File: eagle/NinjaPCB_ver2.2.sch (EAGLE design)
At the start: 60 parts, among them IC3 ANALOGSW_AD_SOT23-6, IC6 NAU7802, J2 ATX24, J3 HEATER, J4 HEATER_TEMP, Q1 S8550, Q2 IRF520NPBF, Q3 IRF520NPBF, Q4 S8550, Q5 IRF520NPBF, Q6 S8550, Q7 S8550, Q8 S8550, U1 CJT1117-3.3-SOT223

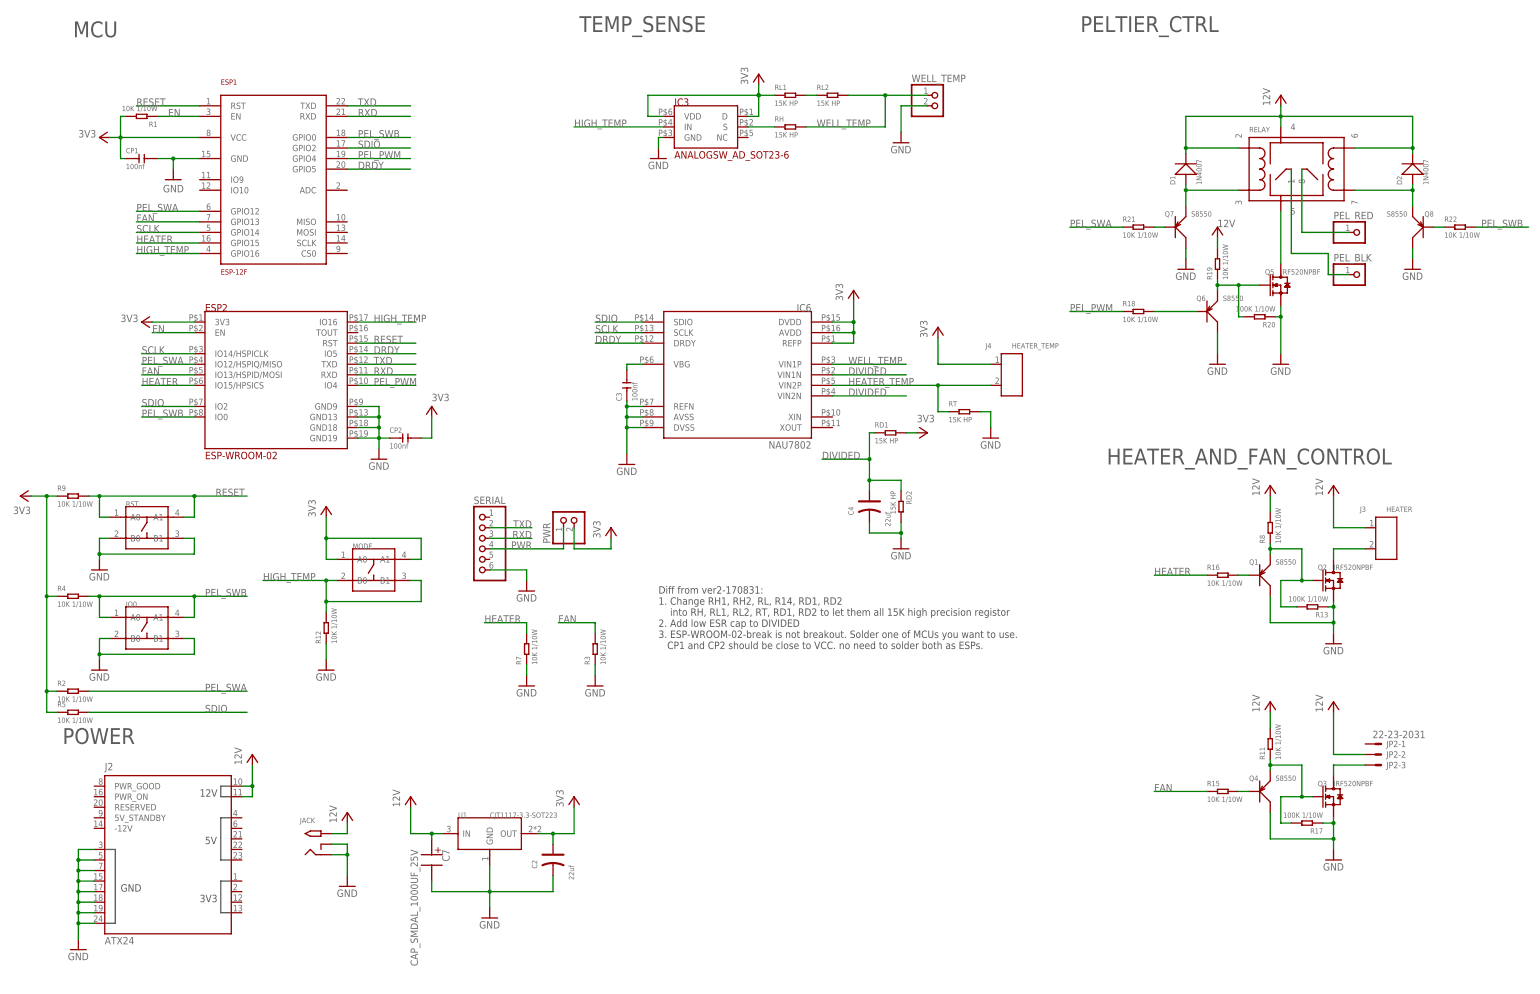
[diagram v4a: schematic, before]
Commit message: replace 2d data to ver2 dxf
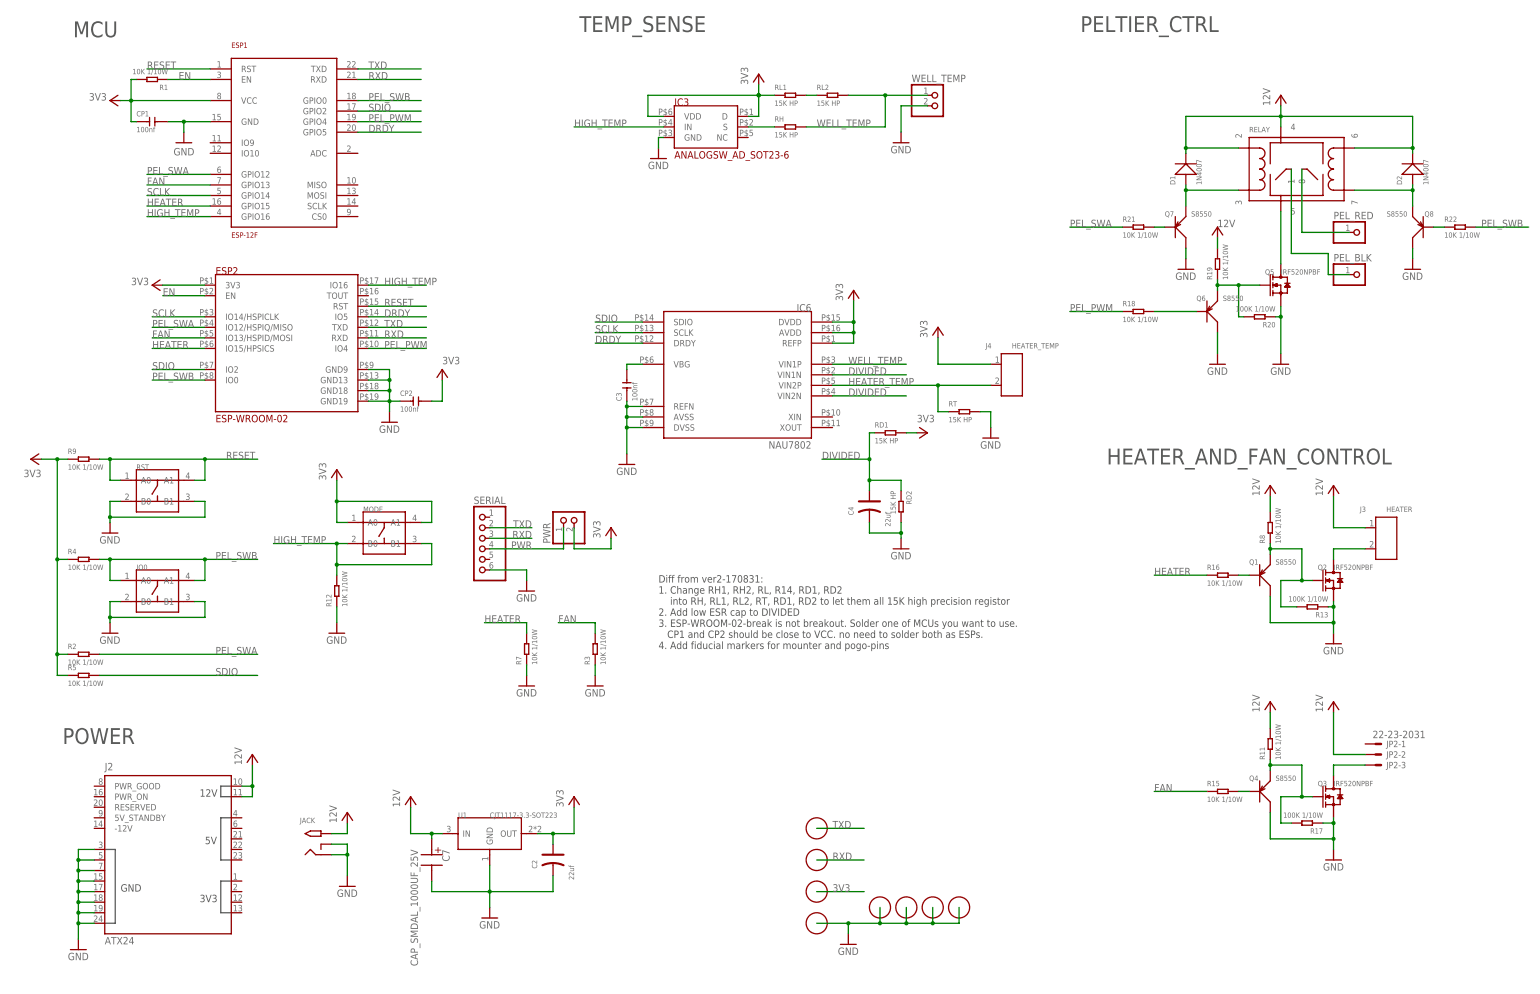
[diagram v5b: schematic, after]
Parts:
- added U$1, U$2, U$3, U$4, U$5, U$6, U$7, U$8: FIDUCIAL, adafruit:FIDUCIAL
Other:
- note added: "Diff from ver2-170831: 1. Change RH1, RH2, RL, R14, RD1, RD2 into RH, RL1, RL2, RT, RD1, RD2 to let them all 15K high precision registor 2. Add low ESR cap to DIVIDED 3. ESP-WROOM-02-break is not breakout. Solder one of MCUs you want to use. CP1 and CP2 should be close to VCC. no need to solder both as ESPs. 4. Add fiducial markers for mounter and pogo-pins"
- note removed: "Diff from ver2-170831: 1. Change RH1, RH2, RL, R14, RD1, RD2 into RH, RL1, RL2, RT, RD1, RD2 to let them all 15K high precision registor 2. Add low ESR cap to DIVIDED 3. ESP-WROOM-02-break is not breakout. Solder one of MCUs you want to use. CP1 and CP2 should be close to VCC. no need to solder both as ESPs."
- moved on the sheet: CP1, CP2, ESP1, ESP2, IO0, MODE, R1, R12, R2, R4, R5, R9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

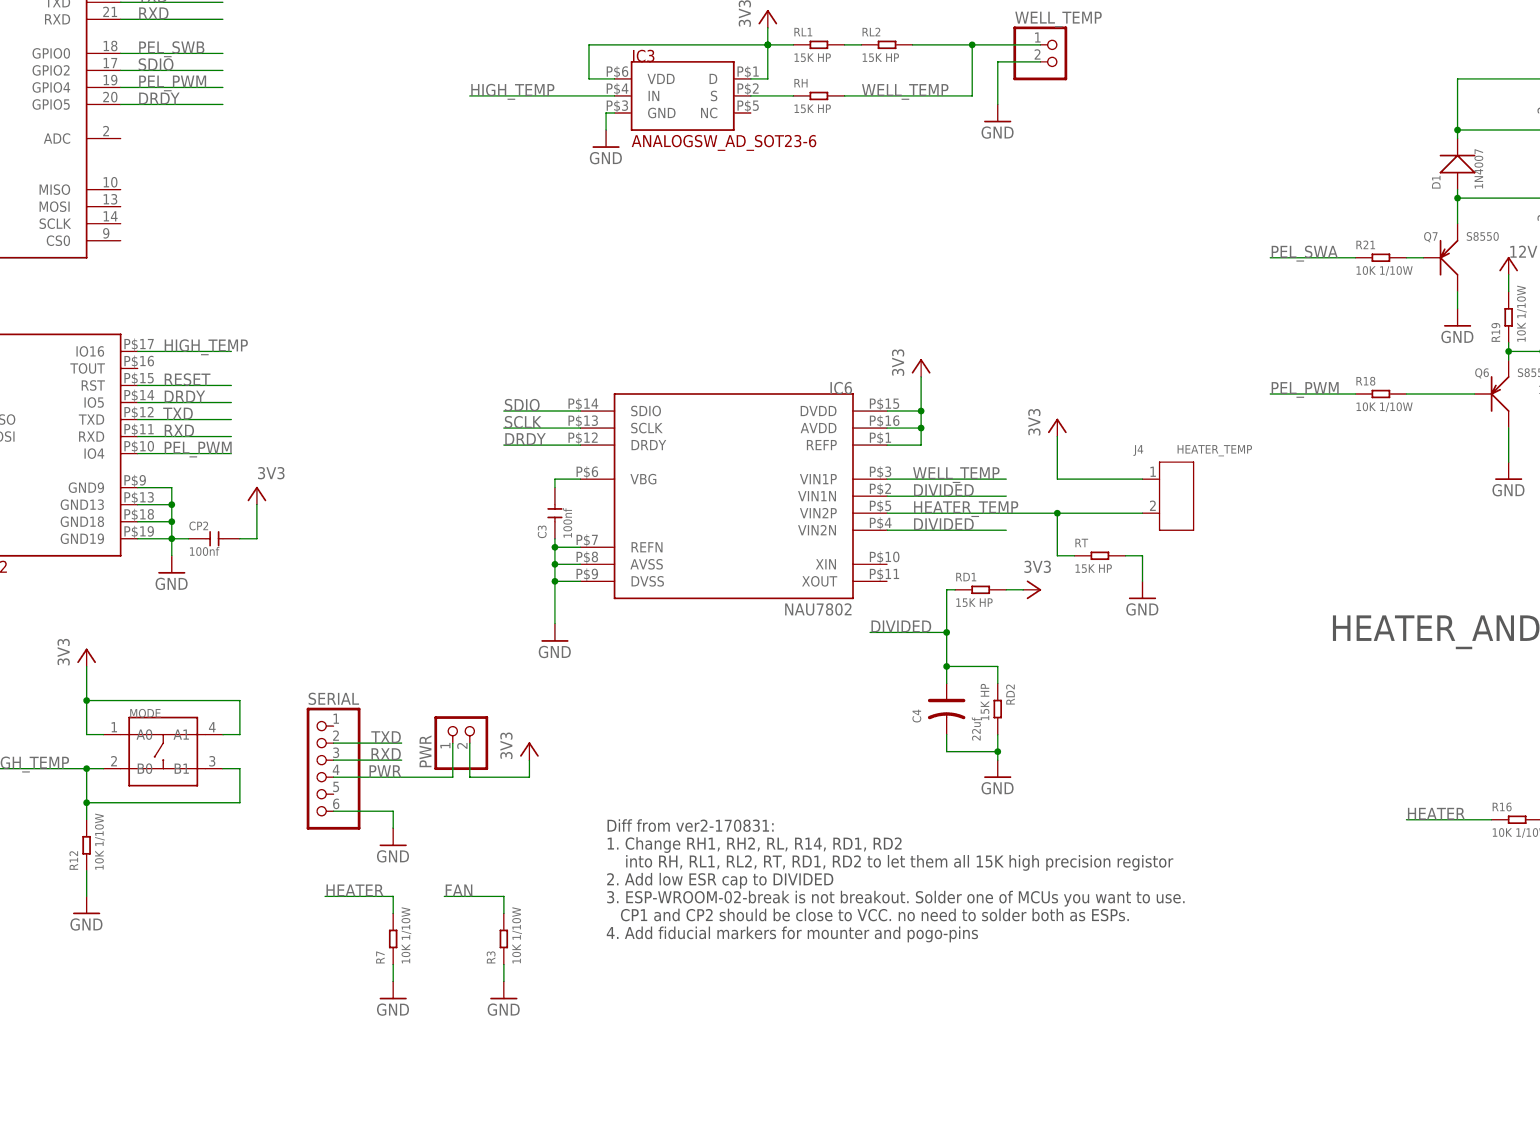
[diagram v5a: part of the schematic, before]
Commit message: add MODE jumper to use same source for 4x4 and 2x2
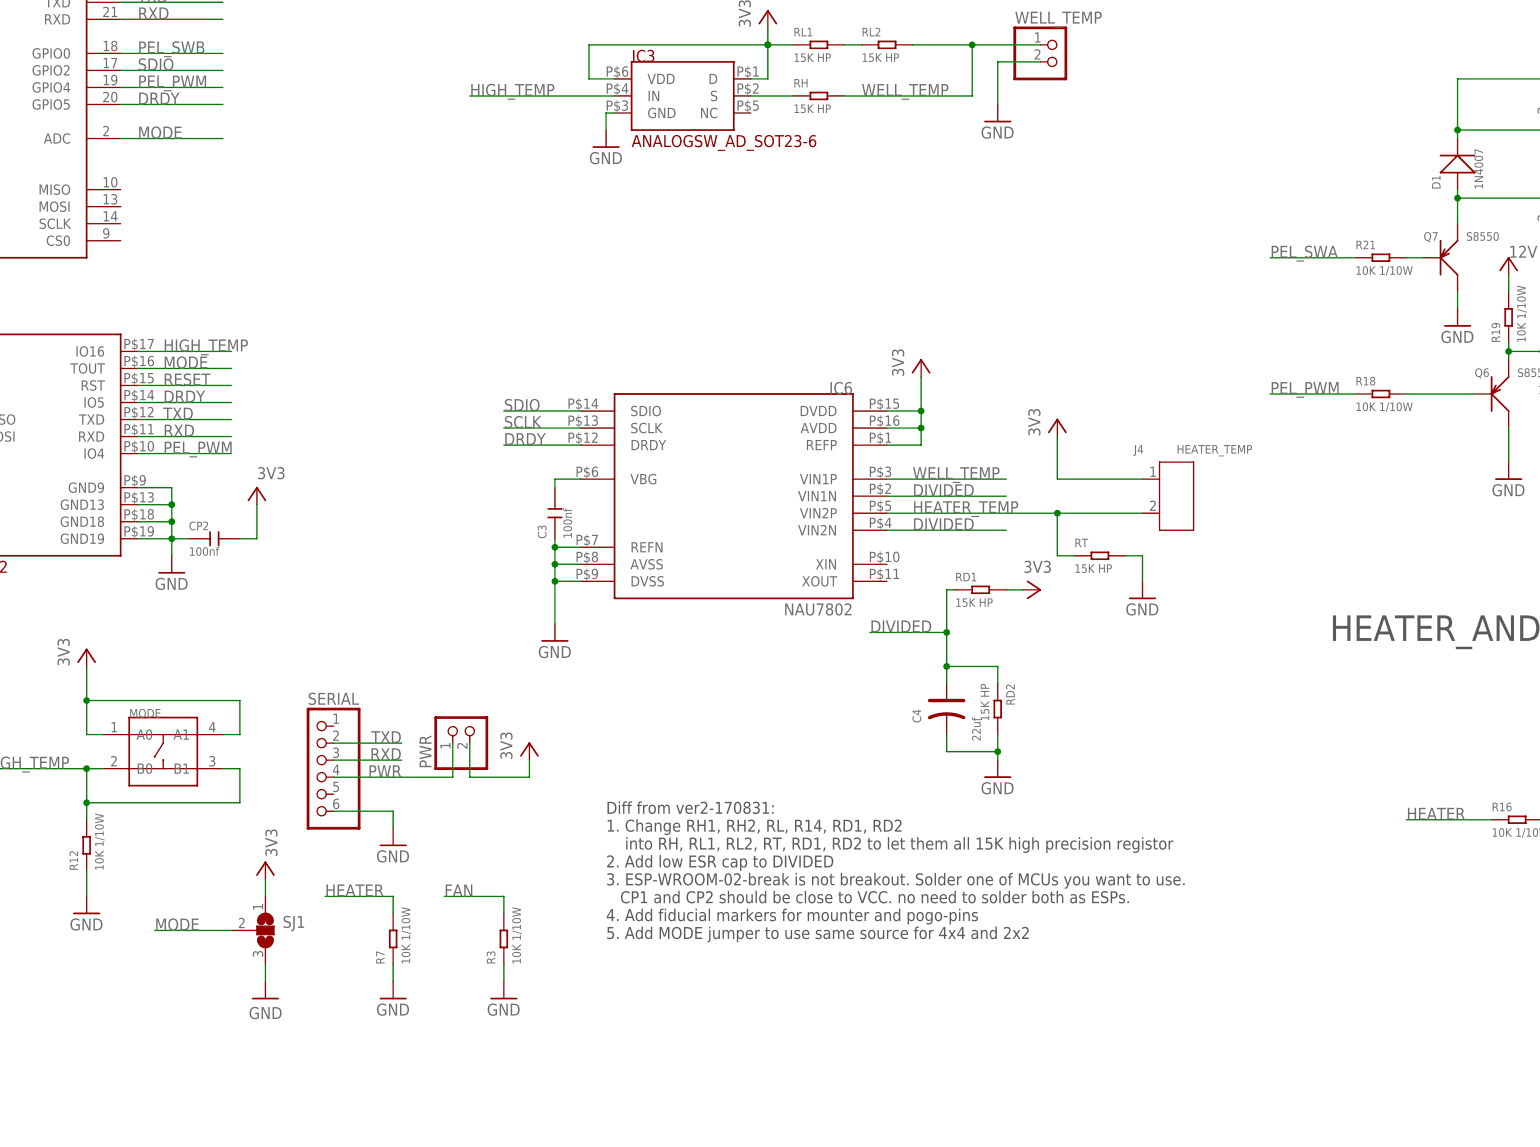
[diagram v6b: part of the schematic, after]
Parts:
- added SJ1: (no value), jumper:SJ2W
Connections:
- new net MODE: ESP1.ADC, ESP2.TOUT, SJ1.2
- net 3V3: now also SJ1.1
- net GND: now also SJ1.3
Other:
- note added: "Diff from ver2-170831: 1. Change RH1, RH2, RL, R14, RD1, RD2 into RH, RL1, RL2, RT, RD1, RD2 to let them all 15K high precision registor 2. Add low ESR cap to DIVIDED 3. ESP-WROOM-02-break is not breakout. Solder one of MCUs you want to use. CP1 and CP2 should be close to VCC. no need to solder both as ESPs. 4. Add fiducial markers for mounter and pogo-pins 5. Add MODE jumper to use same source f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"
- note removed: "Diff from ver2-170831: 1. Change RH1, RH2, RL, R14, RD1, RD2 into RH, RL1, RL2, RT, RD1, RD2 to let them all 15K high precision registor 2. Add low ESR cap to DIVIDED 3. ESP-WROOM-02-break is not breakout. Solder one of MCUs you want to use. CP1 and CP2 should be close to VCC. no need to solder both as ESPs. 4. Add fiducial markers for mounter and pogo-pins"

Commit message: add MooMoo ones
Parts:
- added R10, R14: 10K 1/10W, Seeed-Resistor:SMD-RES-10K-5%-1/10W(0603)
- added R6: 100K 1/10W, Seeed-Resistor:SMD-RES-100K-5%-1/10W(0603)
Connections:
- new net N$8: R10.1, R6.2, SJ1.1
- new net N$9: R14.2, SJ1.3
- net 3V3: now also R10.2; no longer SJ1.1
- net GND: now also R14.1, R6.1; no longer SJ1.3
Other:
- moved on the sheet: SJ1
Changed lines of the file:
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@@
 <part name="GND24" library="supply1" deviceset="GND" device=""/>
 <part name="SJ1" library="jumper" deviceset="SJ2W" device=""/>
+<part name="R6" library="Seeed-Resistor" deviceset="SMD-RES-100K-5%-1/10W(0603)" device="" value="100K 1/10W"/>
+<part name="R10" library="Seeed-Resistor" deviceset="SMD-RES-10K-5%-1/10W(0603)" device="" value="10K 1/10W"/>
+<part name="R14" library="Seeed-Resistor" deviceset="SMD-RES-10K-5%-1/10W(0603)" device="" value="10K 1/10W"/>
 </parts>
 <sheets>
@@
 <instance part="U$8" gate="G$1" x="205.74" y="48.26"/>
 <instance part="GND16" gate="1" x="213.36" y="20.32"/>
-<instance part="3V9" gate="VCC" x="116.84" y="102.87" smashed="yes">
-<attribute name="VALUE" x="116.84" y="107.95" size="1.778" layer="96" rot="R270"/>
+<instance part="3V9" gate="VCC" x="118.11" y="102.87" smashed="yes">
+<attribute name="VALUE" x="118.11" y="107.95" size="1.778" layer="96" rot="R270"/>
 </instance>
-<instance part="GND24" gate="1" x="116.84" y="82.55" smashed="yes">
-<attribute name="VALUE" x="119.38" y="81.28" size="1.778" layer="96" rot="R180"/>
+<instance part="GND24" gate="1" x="110.49" y="59.69" smashed="yes">
+<attribute name="VALUE" x="113.03" y="58.42" size="1.778" layer="96" rot="R180"/>
 </instance>
-<instance part="SJ1" gate="G$1" x="116.84" y="92.71"/>
+<instance part="SJ1" gate="G$1" x="110.49" y="78.74"/>
+<instance part="R6" gate="G$1" x="118.11" y="78.74" rot="R90"/>
+<instance part="R10" gate="G$1" x="118.11" y="93.98" rot="R90"/>
+<instance part="R14" gate="G$1" x="110.49" y="68.58" rot="R90"/>
 </instances>
 <busses>
@@
 </segment>
 <segment>
-<pinref part="SJ1" gate="G$1" pin="3"/>
 <pinref part="GND24" gate="1" pin="GND"/>
-<wire x1="116.84" y1="87.63" x2="116.84" y2="85.09" width="0.1524" layer="91"/>
+<pinref part="R6" gate="G$1" pin="1"/>
+<wire x1="110.49" y1="63.5" x2="110.49" y2="62.23" width="0.1524" layer="91"/>
+<wire x1="118.11" y1="74.93" x2="118.11" y2="63.5" width="0.1524" layer="91"/>
+<wire x1="118.11" y1="63.5" x2="110.49" y2="63.5" width="0.1524" layer="91"/>
+<pinref part="R14" gate="G$1" pin="1"/>
+<wire x1="110.49" y1="64.77" x2="110.49" y2="63.5" width="0.1524" layer="91"/>
+<junction x="110.49" y="63.5"/>
 </segment>
 </net>
@@
 </segment>
 <segment>
+<pinref part="R10" gate="G$1" pin="2"/>
 <pinref part="3V9" gate="VCC" pin="VCC"/>
-<pinref part="SJ1" gate="G$1" pin="1"/>
-<wire x1="116.84" y1="100.33" x2="116.84" y2="97.79" width="0.1524" layer="91"/>
+<wire x1="118.11" y1="97.79" x2="118.11" y2="100.33" width="0.1524" layer="91"/>
 </segment>
 </net>
@@
 </segment>
 <segment>
-<wire x1="100.33" y1="92.71" x2="111.76" y2="92.71" width="0.1524" layer="91"/>
-<label x="100.33" y="92.71" size="1.778" layer="95"/>
+<wire x1="95.25" y1="78.74" x2="105.41" y2="78.74" width="0.1524" layer="91"/>
+<label x="95.25" y="78.74" size="1.778" layer="95"/>
 <pinref part="SJ1" gate="G$1" pin="2"/>
 </segment>
 </net>
+<net name="N$8" class="0">
+<segment>
+<pinref part="R6" gate="G$1" pin="2"/>
+<pinref part="R10" gate="G$1" pin="1"/>
+<wire x1="118.11" y1="82.55" x2="118.11" y2="86.36" width="0.1524" layer="91"/>
+<wire x1="118.11" y1="86.36" x2="118.11" y2="90.17" width="0.1524" layer="91"/>
+<pinref part="SJ1" gate="G$1" pin="1"/>
+<wire x1="118.11" y1="86.36" x2="110.49" y2="86.36" width="0.1524" layer="91"/>
+<wire x1="110.49" y1="86.36" x2="110.49" y2="83.82" width="0.1524" layer="91"/>
+<junction x="118.11" y="86.36"/>
+</segment>
+</net>
+<net name="N$9" class="0">
+<segment>
+<pinref part="SJ1" gate="G$1" pin="3"/>
+<pinref part="R14" gate="G$1" pin="2"/>
+<wire x1="110.49" y1="73.66" x2="110.49" y2="72.39" width="0.1524" layer="91"/>
+</segment>
+</net>
